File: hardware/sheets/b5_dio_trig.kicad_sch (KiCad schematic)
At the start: 41 parts, among them J501 KF301-5.0-2P, J502 KF301-5.0-2P, J503 KF301-5.0-2P, J504 KF301-5.0-2P, J505 KF301-5.0-2P, J506 KF301-5.0-2P, J507 KF301-5.0-2P, U501 SN74AHCT541PWR, U502 74HCT125PW, U503 SN74LVC1T45DBVR, U504 SN74LVC1G17DBVR, U505 TCA9535PWR, X501 10 MHz TCXO

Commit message: hardware: chip resistors and ceramic capacitors on KiCad standard footprints (Decision #47); schematic, library and gapped copies regenerated, ERC 0 errors
Co-Authored-By: Claude Fable 5.1 <noreply@anthropic.com>
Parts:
- C501, C502, C503, C504, C505, C506, C507: footprint class_board:C0603 -> Capacitor_SMD:C_0603_1608Metric
- R501, R502, R503, R504, R505, R506, R507, R508, R509, R510, R511, R512, R513, R514, R515: footprint class_board:R0603 -> Resistor_SMD:R_0603_1608Metric

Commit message: hardware: panel stacked on the back (180 x 100, three 2x20 headers, 17 SMA, TTL strip, TX terminal, Qwiic); TTL/fast/TX-coil/Qwiic connectors leave the main board; mains-safe relay channels (JQC-3FF 10 A, MAINS net class + DRC rules); library, sheets, gapped copies, docs regenerated; ERC 0 errors
Decisions #45-#50 in the course repo. The main-board PCB is unchanged: Update PCB from Schematic, header placement, relay re-spacing and connector rotation are the instructor's GUI steps on the master.

Co-Authored-By: Claude Fable 5.1 <noreply@anthropic.com>
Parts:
- removed J501, J502, J503, J504, J505, J506, J507: KF301-5.0-2P, class_board:CONN-TH_P5.00_KF301-5.0-2P, symbol class_board:KF301-5.0-2P
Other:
- note added: "74AHCT541 (TTL-compatible inputs accept 3.3 V) buffers DIO1..8 to 5 V; 1 k series per output limits a shorted output to 5 mA (students!). Outputs are static/slow (kHz): 1 k x 100 pF cable = 100 ns. v0.8: TTL1..8 and FASTTTL1/2 leave on the panel link, not on board-edge terminals."
- note added: "74HCT125: FAST_OUT1/2 (MCPWM/RMT) -> 49.9 R series -> the panel link -> the two fast SMAs on the panel; drive +-6 mA rated, so a 50 R termination gives ~1 V: fast outs are for high-impedance TTL loads."
- note added: "FASTTTL1/2 leave this sheet as global labels -> panel link J7 -> the two fast SMAs"
- note added: "TTL1..TTL8 leave this sheet as global labels -> panel link J7 -> the 10-way screw-terminal"
- note added: "on the front panel (49.9 R series). The edge terminals J506/J507 are gone (v0.8)."
- note added: "strip on the front panel (TTL1..8 + 2 x GND). The board-edge terminals J501-J505 are gone (v0.8)."
- note removed: "74AHCT541 (TTL-compatible inputs accept 3.3 V) buffers DIO1..8 to 5 V; 1 k series per output limits a shorted output to 5 mA (students!). Outputs are static/slow (kHz): 1 k x 100 pF cable = 100 ns."
- note removed: "74HCT125: FAST_OUT1/2 (MCPWM/RMT) -> 49.9 R series -> terminals; drive +-6 mA rated, so a 50 R termination gives ~1 V: fast outs are for high-impedance TTL loads."
- note removed: "J501-J504: TTL1..TTL8 (5 V TTL out, 1 k series); J505: GND GND"
- note removed: "J506/J507: FASTTTL1/2 + GND (5 V TTL, 49.9 R series)"

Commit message: v0.7d: relays and mains removed, MODULE OUT 1-7 (5 V TTL) on a shrouded 2x6 header on the front panel, isolated inputs moved to the panel, section C = the front-panel board (4-layer, 18 mm SMA grid, OLED clear of headers, unrouted student copy), main board re-placed; workbook, tutor guide, firmware docs, hardware docs updated (Decision #58)
Co-Authored-By: Claude Fable 5.1 <noreply@anthropic.com>
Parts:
- removed TP502, TP503, TP504: TP, class_board:TestPoint_Pad_D1.5mm, symbol class_board:TestPoint
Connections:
- net EXP_P15 renamed MOD5
- net EXP_P16 renamed MOD6
- net EXP_P17 renamed MOD7
- net RLY_IN1 renamed MOD1
- net RLY_IN2 renamed MOD2
- net RLY_IN3 renamed MOD3
- net RLY_IN4 renamed MOD4
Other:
- note added: "P00..P07 = DIO1..8 into the 74AHCT541 above; P10..P13 and P15..P17 = MODULE OUT 1..7, the 3.3 V module outputs, to the panel link J8 (v0.7d)."
- note added: "P14 is NOT free: it is EXP_P14, the /CLR of the 74HC74 Johnson counter on the NMR receiver sheet (TP501 is its test point). MODULE OUT 8 is"
- note added: "mapping is unchanged. Every port is an input after power-up and after a reset: the pull-down on the panel buffer decides the state of a module."
- note added: "reserved: J8 pin 33 is not connected on this board and the panel pulls it down. MOD1..MOD4 keep the ports the relay gates used, so the firmware"
- note added: "v0.7: DIO1..8 keep their names but are no longer MCU pins — they come from the TCA9535 I2C expander U505 (address 0x20, A0 = A1 = A2 = GND), P00..P07. The 541 runs at +5V_RAW while the expander drives 3.3 V: the AHCT TTL thresholds (VIH 2.0 V) accept that. v0.7d: P10..P13 and P15..P17 = MODULE OUT 1..7 to the panel link J8 (P10..P13 are the ports the four relay gates used); P14 stays EXP_P14, the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"
- note removed: "Every port is an input after power-up and after a reset: the relay gate pull-downs (B4) are what set the safe state."
- note removed: "P00..P07 = DIO1..8 into the 74AHCT541 above, P10..P13 = RLY_IN1..4 to the relay gates (B4), P14..P17 spare on TP501..TP504."
- note removed: "v0.7: DIO1..8 keep their names but are no longer MCU pins — they come from the TCA9535 I2C expander U505 (address 0x20, A0 = A1 = A2 = GND), P00..P07. The 541 runs at +5V_RAW while the expander drives 3.3 V: the AHCT TTL thresholds (VIH 2.0 V) accept that. P10..P13 = RLY_IN1..4 (relay gates, B4), P14..P17 = spare on test points EXP_P14..P17."

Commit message: Schematic spacing rework: all nine sheets checker-clean, netlist fixes (LM66100 inputs off GND, TCXO divider joined), arrow rails, A2 for b5/c_switch/nmr_tx/nmr_rx; sch_check.py + net_diff.py; renders in docs/sch
Co-Authored-By: Claude Fable 5.1 <noreply@anthropic.com>
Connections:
- net at C505.2, U504.2 (A): now also R514.2, R515.1
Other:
- note added: "/CLR of the 74HC74 Johnson counter on the NMR receiver sheet (TP501 is its test point). MODULE OUT 8 is reserved: J8 pin 33 is not connected on this"
- note added: "10 MHz timebase option — all parts DNP by default (zero cost);"
- note added: "74AHCT541 (TTL-compatible inputs accept 3.3 V) buffers DIO1..8 to 5 V; 1 k series per output limits a shorted output to 5 mA (students!). Outputs are static/slow (kHz): 1 k x 100 pF cable = 100 ns. v0.8: TTL1..8 and FASTTTL1/2 leave on the panel link, not on"
- note added: "74AHCT541 above; P10..P13 and P15..P17 = MODULE OUT 1..7, the 3.3 V module outputs, to the panel link J8 (v0.7d). P14 is NOT free: it is EXP_P14, the"
- note added: "FASTTTL1/2 leave this sheet as global labels -> panel link J7 ->"
- note added: "JP501 open until a firmware use exists"
- note added: "TTL1..TTL8 leave this sheet as global labels -> panel link J7 -> the 10-way screw-terminal strip"
- note added: "The edge terminals J506/J507 are gone (v0.8)."
- note added: "U505 TCA9535 (TSSOP-24, address 0x20, A0 = A1 = A2 = GND): the I2C port expander that replaced 12 direct GPIO in v0.7 — P00..P07 = DIO1..8 into the"
- note added: "after power-up and after a reset: the pull-down on the panel buffer decides the state of a module."
- note added: "board and the panel pulls it down. MOD1..MOD4 keep the ports the relay gates used, so the firmware mapping is unchanged. Every port is an input"
- note added: "board-edge terminals."
- note added: "on the front panel (TTL1..8 + 2 x GND). The board-edge terminals J501-J505 are gone (v0.8)."
- note added: "the two fast SMAs on the front panel (49.9 R series)."
- note added: "v0.7: DIO1..8 keep their names but are no longer MCU pins — they come from the TCA9535 I2C expander U505 (address 0x20, A0 = A1 = A2 = GND), P00..P07. The 541 runs at +5V_RAW while the expander drives 3.3 V: the AHCT TTL thresholds (VIH 2.0 V) accept that."
- note added: "v0.7d: P10..P13 and P15..P17 = MODULE OUT 1..7 to the panel link J8 (P10..P13 are the ports the four relay gates used); P14 stays EXP_P14, the Johnson-counter /CLR of the NMR receiver; MODULE OUT 8 is reserved (J8 pin 33 not connected)."
- note removed: "10 MHz timebase option — all parts DNP by default (zero cost); JP501 open until a firmware use exists"
- note removed: "74AHCT541 (TTL-compatible inputs accept 3.3 V) buffers DIO1..8 to 5 V; 1 k series per output limits a shorted output to 5 mA (students!). Outputs are static/slow (kHz): 1 k x 100 pF cable = 100 ns. v0.8: TTL1..8 and FASTTTL1/2 leave on the panel link, not on board-edge terminals."
- note removed: "FASTTTL1/2 leave this sheet as global labels -> panel link J7 -> the two fast SMAs"
- note removed: "P00..P07 = DIO1..8 into the 74AHCT541 above; P10..P13 and P15..P17 = MODULE OUT 1..7, the 3.3 V module outputs, to the panel link J8 (v0.7d)."
- note removed: "P14 is NOT free: it is EXP_P14, the /CLR of the 74HC74 Johnson counter on the NMR receiver sheet (TP501 is its test point). MODULE OUT 8 is"
- note removed: "TTL1..TTL8 leave this sheet as global labels -> panel link J7 -> the 10-way screw-terminal"
- note removed: "U505 TCA9535 (TSSOP-24, address 0x20, A0 = A1 = A2 = GND): the I2C port expander that replaced 12 direct GPIO in v0.7 —"
- note removed: "mapping is unchanged. Every port is an input after power-up and after a reset: the pull-down on the panel buffer decides the state of a module."
- note removed: "on the front panel (49.9 R series). The edge terminals J506/J507 are gone (v0.8)."
- note removed: "reserved: J8 pin 33 is not connected on this board and the panel pulls it down. MOD1..MOD4 keep the ports the relay gates used, so the firmware"
- note removed: "strip on the front panel (TTL1..8 + 2 x GND). The board-edge terminals J501-J505 are gone (v0.8)."
- note removed: "v0.7: DIO1..8 keep their names but are no longer MCU pins — they come from the TCA9535 I2C expander U505 (address 0x20, A0 = A1 = A2 = GND), P00..P07. The 541 runs at +5V_RAW while the expander drives 3.3 V: the AHCT TTL thresholds (VIH 2.0 V) accept that. v0.7d: P10..P13 and P15..P17 = MODULE OUT 1..7 to the panel link J8 (P10..P13 are the ports the four relay gates used); P14 stays EXP_P14, the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"
- moved on the sheet: C501, C502, C503, C504, C505, C506, C507, D501, JP501, R501, R502, R503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

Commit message: Boards as hand-reworked by the instructor 2026-09-18 (Decision #66): three 2x20 links re-placed, jumpers -> headers, TCXO removed, 16 SMA; layout and routing in progress; review in the course repo notes
Co-Authored-By: Claude Fable 5.1 <noreply@anthropic.com>
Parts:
- removed C505: 1nF, Capacitor_SMD:C_0603_1608Metric, symbol class_board:C0603_1nF
- removed C506: 100nF, Capacitor_SMD:C_0603_1608Metric, symbol class_board:C0603_100nF
- removed JP501: SolderJumper_2_Open, class_board:SolderJumper-2_P1.3mm_Open_RoundedPad1.0x1.5mm, symbol class_board:SolderJumper_2_Open
- removed R512, R513, R514, R515: 100k, Resistor_SMD:R_0603_1608Metric, symbol class_board:R0603_100k
- removed U504: SN74LVC1G17DBVR, class_board:SOT-23-5_L3.0-W1.7-P0.95-LS2.8-BR, symbol class_board:SN74LVC1G17DBVR
- removed X501: 10 MHz TCXO, class_board:OSC-SMD_4P-L3.2-W2.5-BL, symbol class_board:1XTV10000MDA
- added J7, J8: Panel link 2x20 female, Connector_PinSocket_2.54mm:PinSocket_2x20_P2.54mm_Vertical, symbol class_board:HDR_2x20_FEMALE
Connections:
- net +3V3: now also J7.5, J8.27, J8.29
- net +5V_RAW: now also J7.1, J7.3
- net FASTTTL1: now also J8.39
- net FASTTTL2: now also J8.37
- net GND: now also J7.10, J7.12, J7.14, J7.16, J7.18, J7.2, J7.20, J7.22, J7.24, J7.26, J7.28, J7.30, J7.32, J7.34, J7.36, J7.38, J7.4, J7.40, J7.6, J7.8, J8.10, J8.12, J8.14, J8.16, J8.18, J8.2, J8.20, J8.22, J8.24, J8.26, J8.28, J8.30, J8.32, J8.34, J8.36, J8.38, J8.4, J8.40, J8.6, J8.8
- net I2C_SCL: now also J8.31
- net I2C_SDA: now also J8.33
- net MOD1: now also J7.23
- net MOD2: now also J7.25
- net MOD3: now also J7.27
- net MOD4: now also J7.29
- net MOD5: now also J7.31
- net MOD6: now also J7.33
- net MOD7: now also J7.35
- net TRIG_5V: now also J8.35
- net TTL1: now also J8.15
- net TTL2: now also J8.13
- net TTL3: now also J8.11
- net TTL4: now also J8.9
- net TTL5: now also J8.7
- net TTL6: now also J8.5
- net TTL7: now also J8.3
- net TTL8: now also J8.1
- new net LED_ACT: J8.23
- new net LED_WIFI: J8.25
- new net OPTO_IN1: J7.15
- new net OPTO_IN2: J7.17
- no-connect marks 4 -> 14
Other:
- note added: "+5V_RAW GND +5V_RAW GND +3V3 GND"
- note added: "1-6"
- note added: "13-18"
- note added: "19-24"
- note added: "25-30"
- note added: "31-36"
- note added: "37-40"
- note added: "7-12"
- note added: "FASTTTL2 GND TRIG_5V GND I2C_SDA GND"
- note added: "GPIO15"
- note added: "GPIO15 GND GPIO43 GND GPIO44 GND"
- note added: "GPIO4"
- note added: "GPIO4 GND GPIO6 GND GPIO7 GND"
- note added: "GPIO43"
- note added: "GPIO44"
- note added: "GPIO6"
- note added: "GPIO7"
- note added: "I2C_SCL GND +3V3 GND LED_PWR GND"
- note added: "J7 - digital, at x = 90 mm on the bottom side"
- note added: "J7 pin table"
- note added: "J8 - rails, GPIO, module outputs, at x = 168 mm on the bottom side"
- note added: "J8 pin table"
- note added: "LED_WIFI GND LED_ACT GND spare GND"
- note added: "MOD1 GND MOD2 GND MOD3 GND"
- note added: "MOD4 GND MOD5 GND MOD6 GND"
- note added: "MOD7 GND spare GND OPTO_IN1 GND"
- note added: "MOD8"
- note added: "OPTO_IN2 GND spare GND"
- note added: "Pins"
- note added: "Signals (odd = signal, even = its return)"
- note added: "TTL1 GND TTL2 GND TTL3 GND"
- note added: "TTL4 GND TTL5 GND TTL6 GND"
- note added: "TTL7 GND TTL8 GND FASTTTL1 GND"
- note added: "spare GND spare GND"
- note removed: "10 MHz timebase option — all parts DNP by default (zero cost);"
- note removed: "JP501 open until a firmware use exists"
- moved on the sheet: C501, C502, C507, R501, R502, R503, R504, R505, R506, R507, R508, R509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

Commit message: WIP main board routing + schematic (instructor), 2026-09-21 05:04
Co-Authored-By: Claude Fable 5.1 <noreply@anthropic.com>
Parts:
- TP501: value TP -> EXP_P14
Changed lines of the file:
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@@
 			)
 		)
-		(property "Value" "TP"
+		(property "Value" "EXP_P14"
 			(at 139.446 116.332 0)
 			(show_name no)

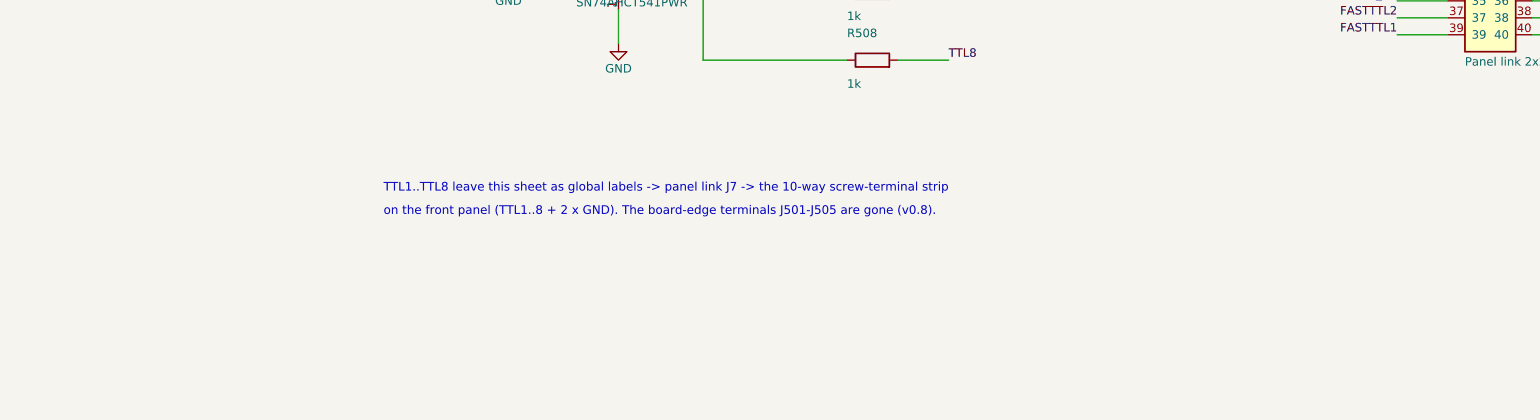
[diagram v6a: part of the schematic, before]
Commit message: Schematic review fixes, part 2 (Konnect): panel RX/AUX labels + SMA labels swapped to match the main board (copper unchanged); TX_VMID -> R820 47k -> TX_IN (C810 couples into TX_IN); Q901 D/S corrected + D932 to +VEXT; R950 10k Q904 gate-source; R712 permanent (J3 pin 1 tied to pin 2); U302/C308 on +5VA; panel 6N137 VCC/VE + C401/C402 on +5V_RAW; R521-R528 DIO pull-downs; front_panel_link sheet removed from the root; change notes on six sheets; panel silk: pairing labels corrected, stale J3 texts deleted, TX/RX/AUX labels fixed, OUT1..7. ERC unchanged (2 cosmetic), panel DRC 0/0; netlist diff = intended changes only
Co-Authored-By: Claude Fable 5.1 <noreply@anthropic.com>
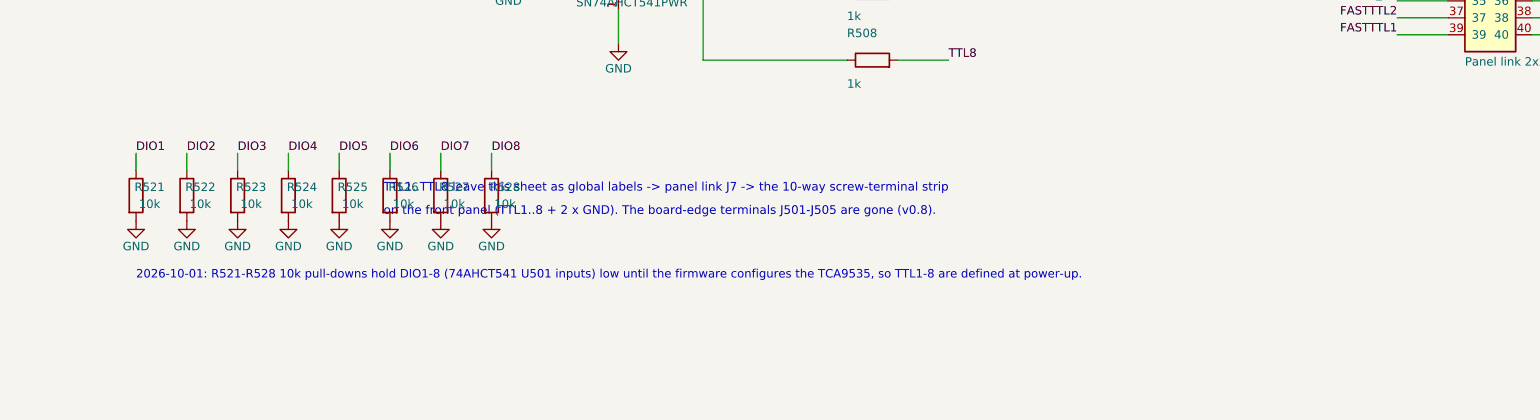
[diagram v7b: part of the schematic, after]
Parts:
- added R521, R522, R523, R524, R525, R526, R527, R528: 10k, Resistor_SMD:R_0603_1608Metric, symbol class_board:R0603_10k
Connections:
- net DIO1: now also R521.1
- net DIO2: now also R522.1
- net DIO3: now also R523.1
- net DIO4: now also R524.1
- net DIO5: now also R525.1
- net DIO6: now also R526.1
- net DIO7: now also R527.1
- net DIO8: now also R528.1
- net GND: now also R521.2, R522.2, R523.2, R524.2, R525.2, R526.2, R527.2, R528.2
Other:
- note added: "2026-10-01: R521-R528 10k pull-downs hold DIO1-8 (74AHCT541 U501 inputs) low until the firmware configures the TCA9535, so TTL1-8 are defined at power-up."

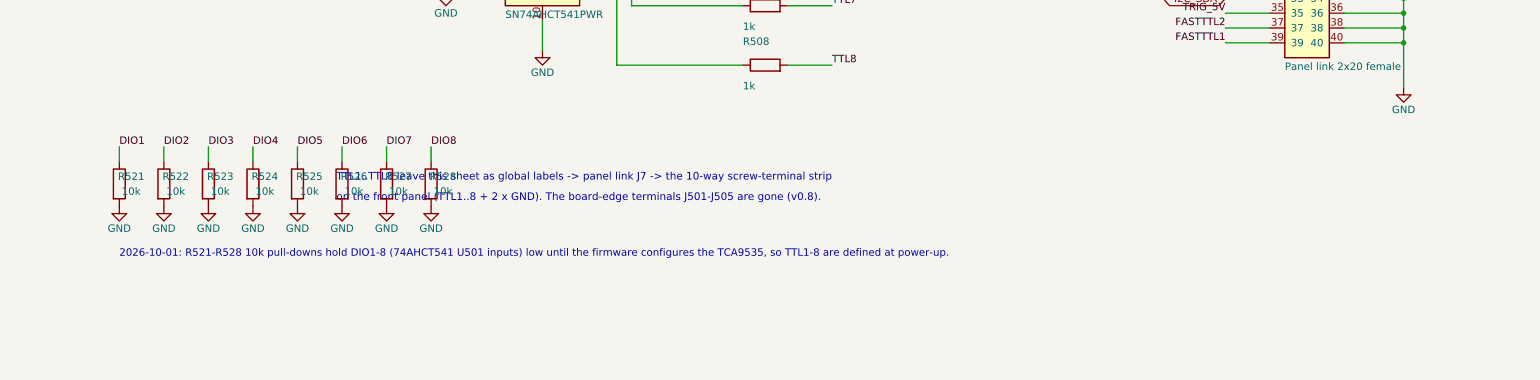
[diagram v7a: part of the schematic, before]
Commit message: b5: DIO1-8 pull-downs as two 4 x 10k arrays RN521/RN522 (0603x4, C29718) instead of R521-R528 (user request); same nets, ERC unchanged
Co-Authored-By: Claude Fable 5.1 <noreply@anthropic.com>
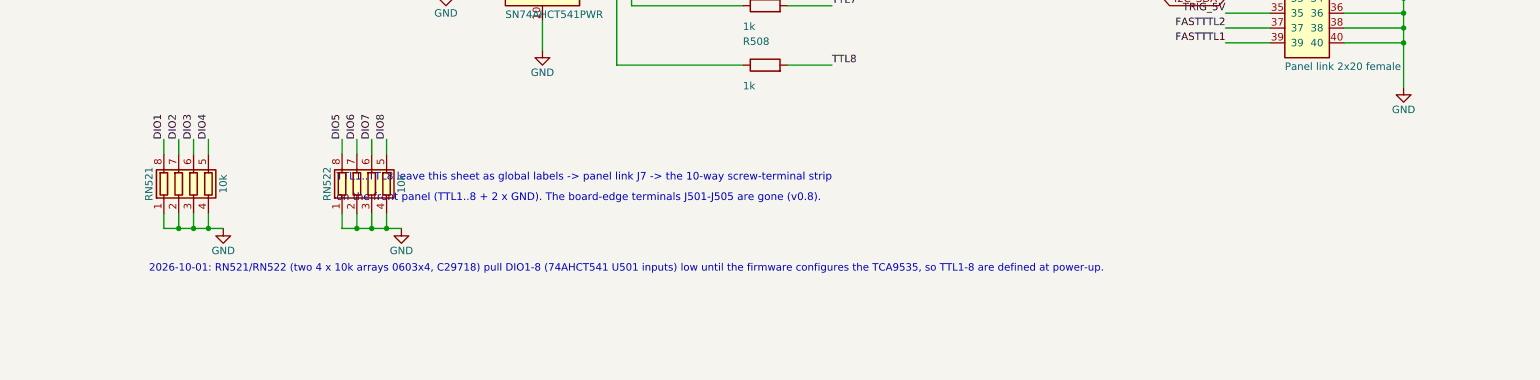
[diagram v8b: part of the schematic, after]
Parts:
- removed R521, R522, R523, R524, R525, R526, R527, R528: 10k, Resistor_SMD:R_0603_1608Metric, symbol class_board:R0603_10k
- added RN521, RN522: 10k, Resistor_SMD:R_Array_Convex_4x0603, symbol Device:R_Pack04
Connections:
- net DIO1: now also RN521.8 (R1.2)
- net DIO2: now also RN521.7 (R2.2)
- net DIO3: now also RN521.6 (R3.2)
- net DIO4: now also RN521.5 (R4.2)
- net DIO5: now also RN522.8 (R1.2)
- net DIO6: now also RN522.7 (R2.2)
- net DIO7: now also RN522.6 (R3.2)
- net DIO8: now also RN522.5 (R4.2)
- net GND: now also RN521.1 (R1.1), RN521.2 (R2.1), RN521.3 (R3.1), RN521.4 (R4.1), RN522.1 (R1.1), RN522.2 (R2.1), RN522.3 (R3.1), RN522.4 (R4.1)
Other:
- note added: "2026-10-01: RN521/RN522 (two 4 x 10k arrays 0603x4, C29718) pull DIO1-8 (74AHCT541 U501 inputs) low until the firmware configures the TCA9535, so TTL1-8 are defined at power-up."
- note removed: "2026-10-01: R521-R528 10k pull-downs hold DIO1-8 (74AHCT541 U501 inputs) low until the firmware configures the TCA9535, so TTL1-8 are defined at power-up."
